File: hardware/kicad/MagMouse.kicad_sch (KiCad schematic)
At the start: 0 parts

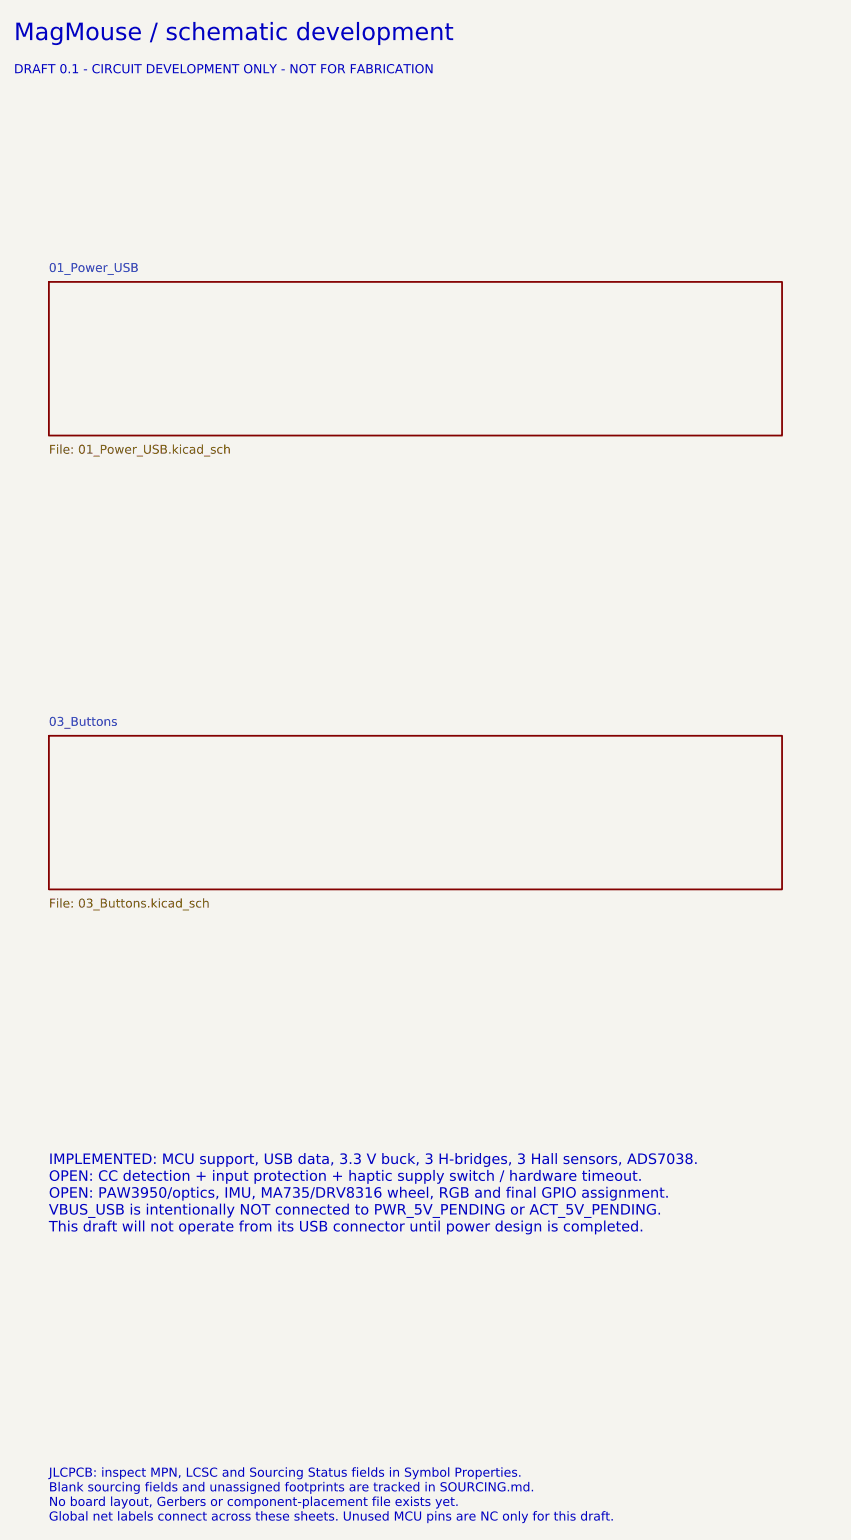
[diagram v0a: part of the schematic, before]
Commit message: Resolve KiCad component sourcing and missing footprints
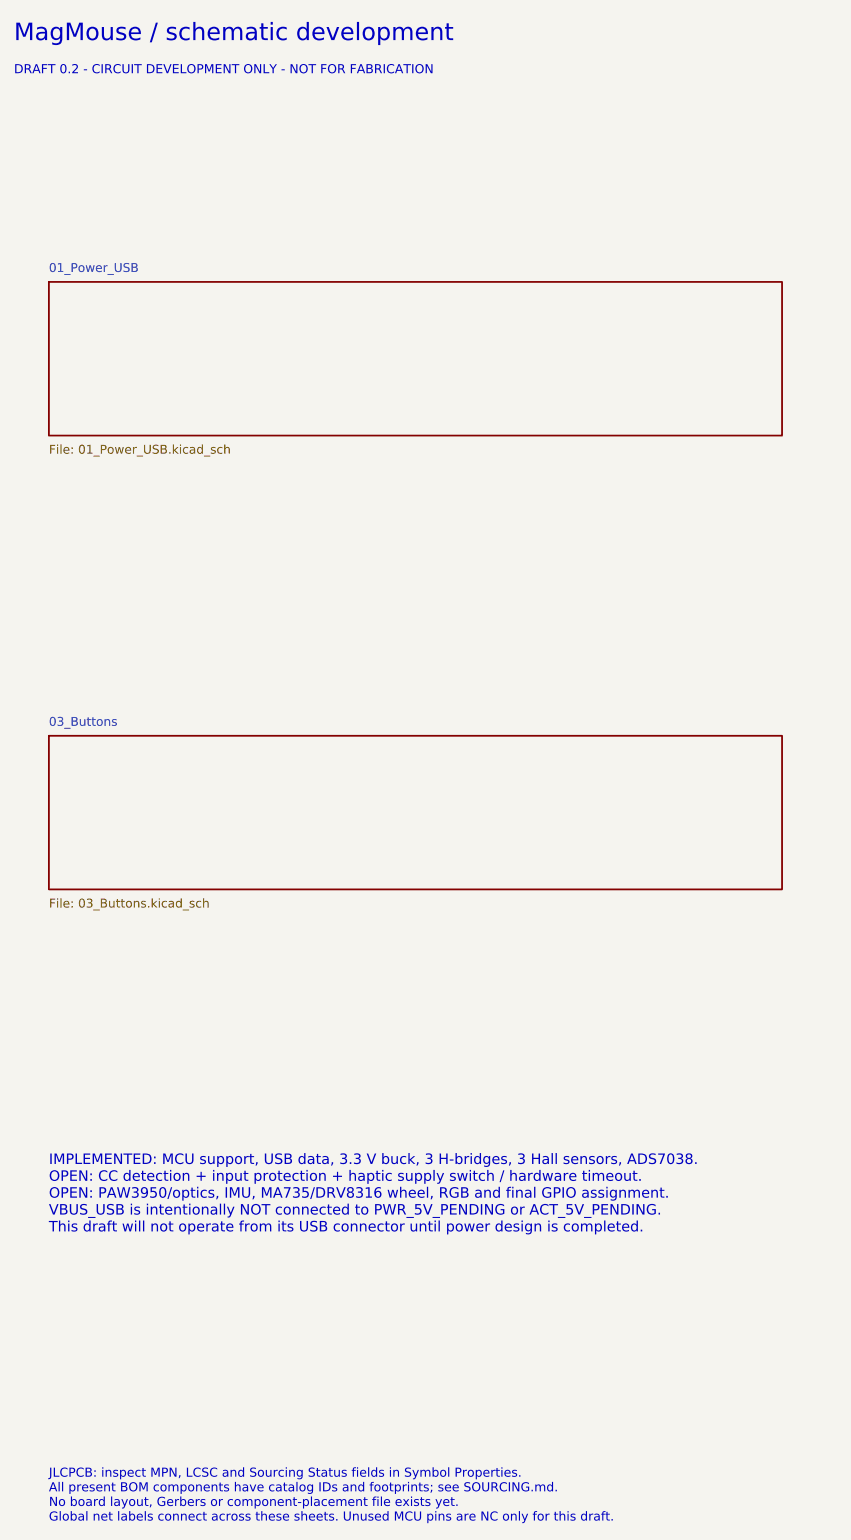
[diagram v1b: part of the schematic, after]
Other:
- note added: "DRAFT 0.2 - CIRCUIT DEVELOPMENT ONLY - NOT FOR FABRICATION"
- note added: "JLCPCB: inspect MPN, LCSC and Sourcing Status fields in Symbol Properties. All present BOM components have catalog IDs and footprints; see SOURCING.md. No board layout, Gerbers or component-placement file exists yet. Global net labels connect across these sheets. Unused MCU pins are NC only for this draft."
- note removed: "DRAFT 0.1 - CIRCUIT DEVELOPMENT ONLY - NOT FOR FABRICATION"
- note removed: "JLCPCB: inspect MPN, LCSC and Sourcing Status fields in Symbol Properties. Blank sourcing fields and unassigned footprints are tracked in SOURCING.md. No board layout, Gerbers or component-placement file exists yet. Global net labels connect across these sheets. Unused MCU pins are NC only for this draft."
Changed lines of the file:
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@@
     (title "MagMouse - MagMouse")
     (date "2026-09-08")
-    (rev "0.1 DRAFT")
+    (rev "0.2 DRAFT")
     (company "MagMouse")
     (comment 1 "NOT FOR FABRICATION - unresolved circuits listed in README.md"))
@@
       (justify left top))
 )
-  (text "DRAFT 0.1 - CIRCUIT DEVELOPMENT ONLY - NOT FOR FABRICATION"
+  (text "DRAFT 0.2 - CIRCUIT DEVELOPMENT ONLY - NOT FOR FABRICATION"
     (at 20 24 0)
     (effects
@@
       (justify left top))
 )
-  (text "JLCPCB: inspect MPN, LCSC and Sourcing Status fields in Symbol Properties.\nBlank sourcing fields and unassigned footprints are tracked in SOURCING.md.\nNo board layout, Gerbers or component-placement file exists yet.\nGlobal net labels connect across these sheets. Unused MCU pins are NC only for this draft."
+  (text "JLCPCB: inspect MPN, LCSC and Sourcing Status fields in Symbol Properties.\nAll present BOM components have catalog IDs and footprints; see SOURCING.md.\nNo board layout, Gerbers or component-placement file exists yet.\nGlobal net labels connect across these sheets. Unused MCU pins are NC only for this draft."
     (at 25 225 0)
     (effects

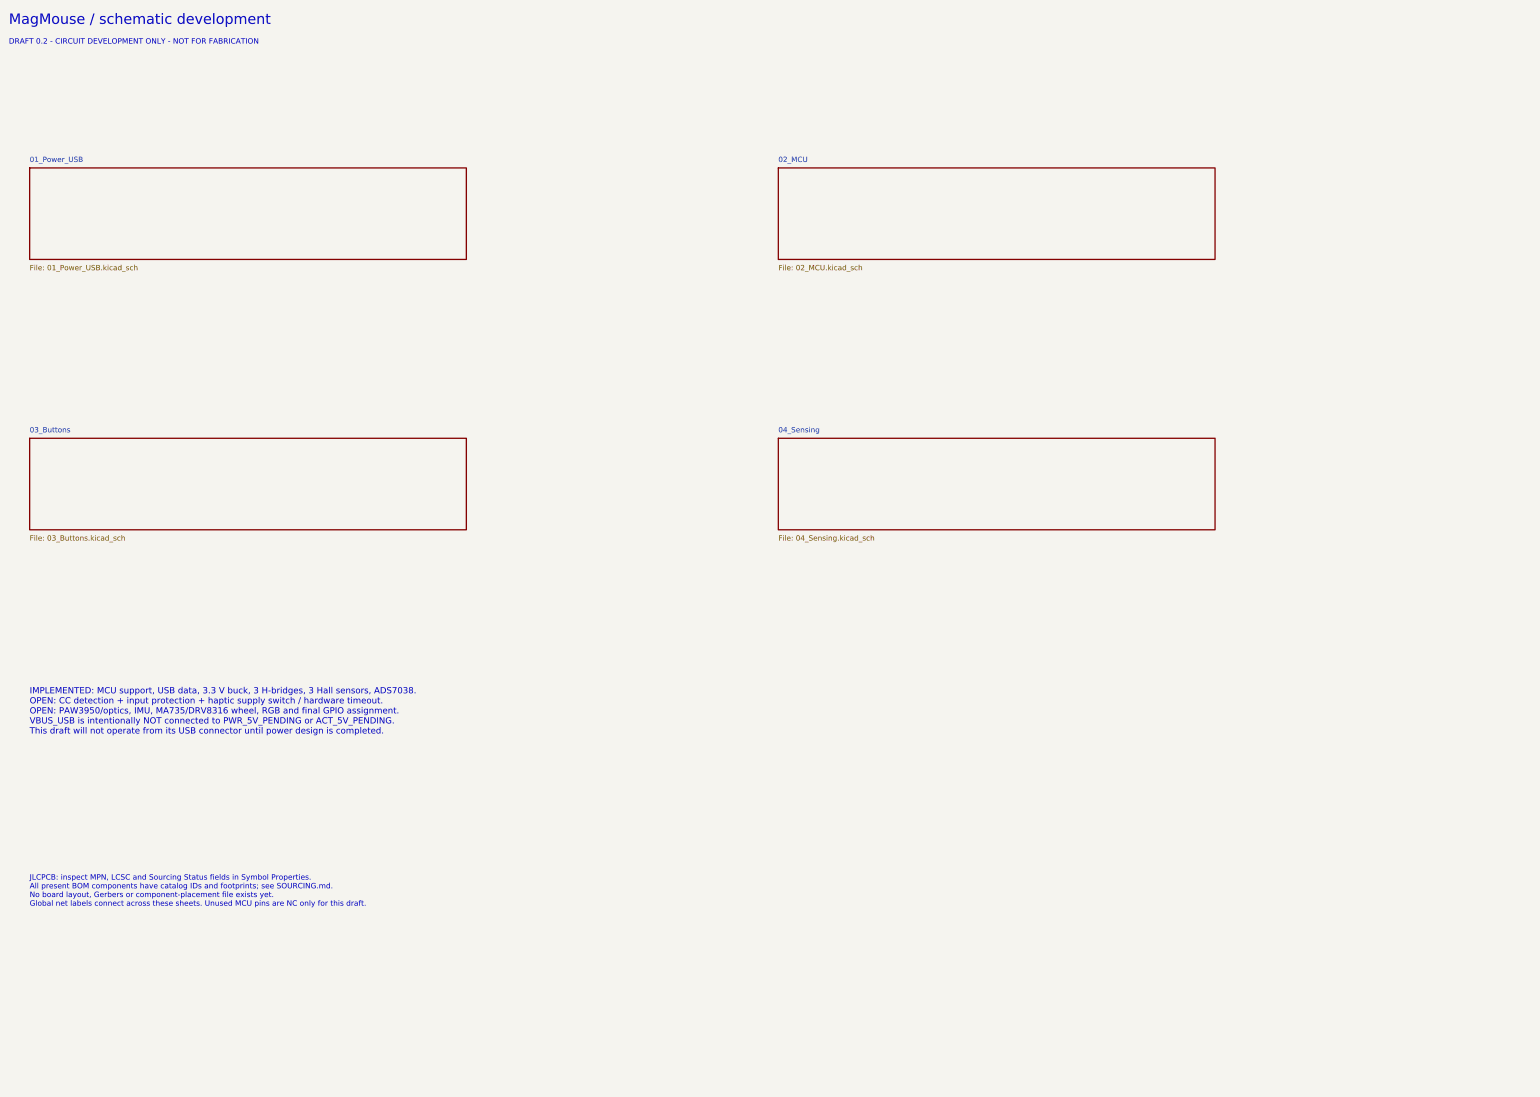
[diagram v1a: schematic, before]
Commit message: Implement USB-C power control schematic and validation
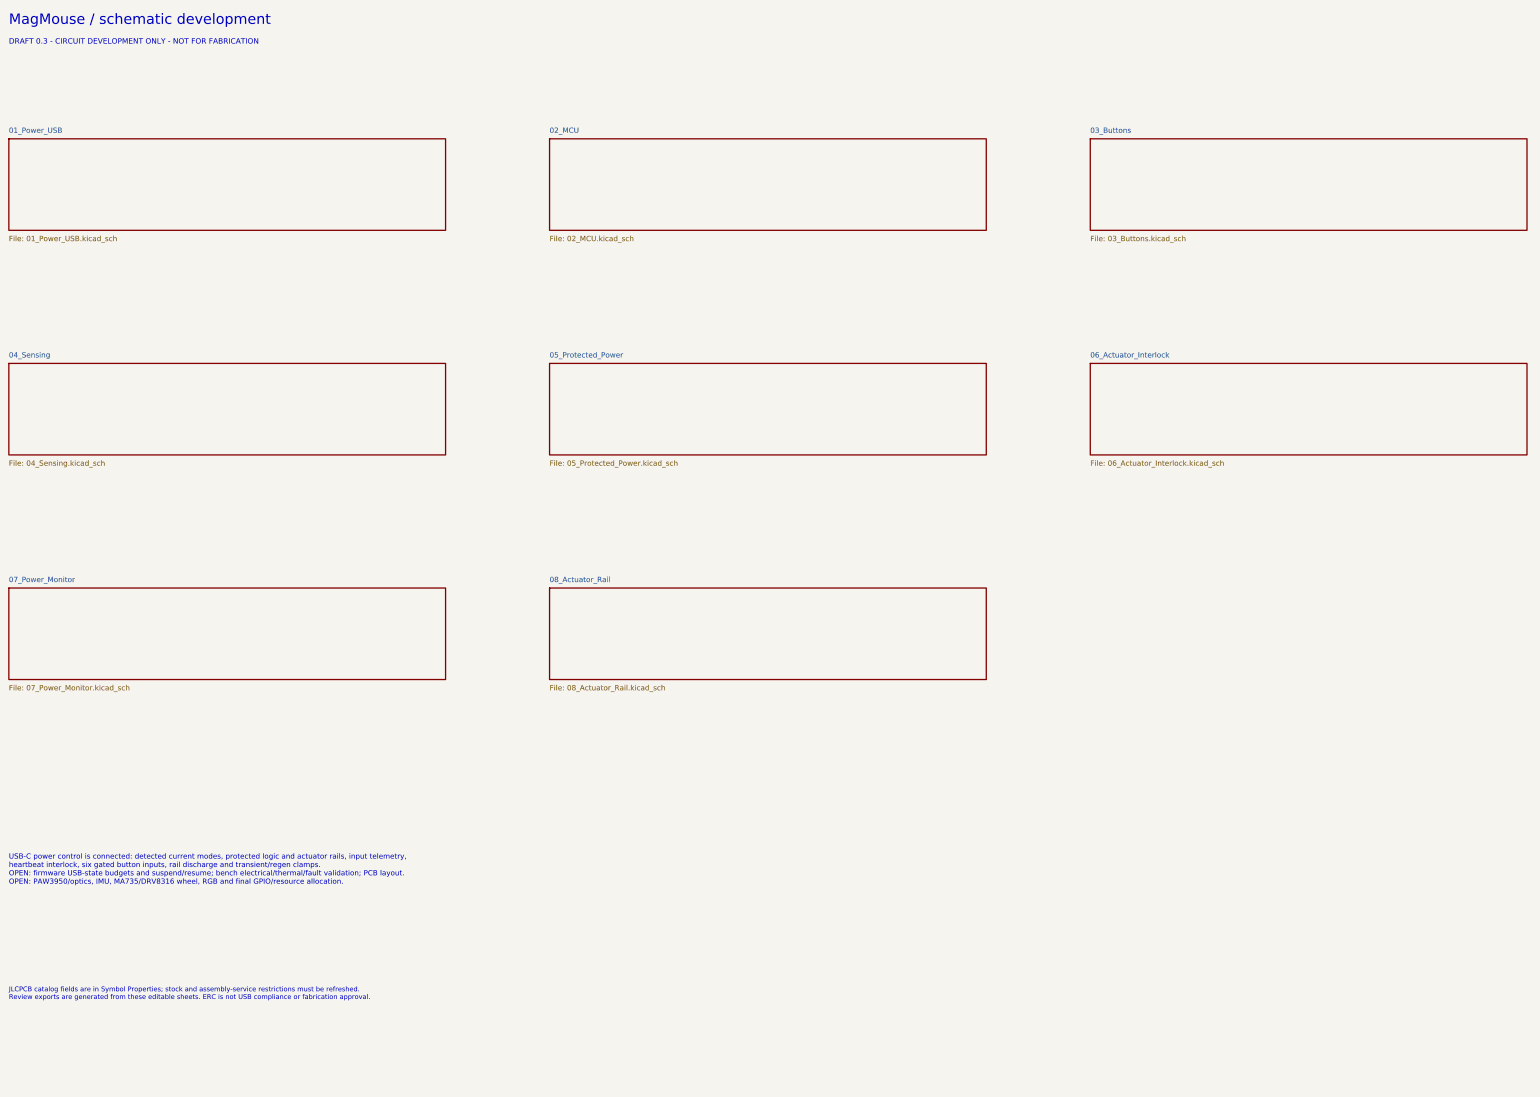
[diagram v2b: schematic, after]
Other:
- added sheet 05_Protected_Power (05_Protected_Power.kicad_sch)
- added sheet 06_Actuator_Interlock (06_Actuator_Interlock.kicad_sch)
- added sheet 07_Power_Monitor (07_Power_Monitor.kicad_sch)
- added sheet 08_Actuator_Rail (08_Actuator_Rail.kicad_sch)
- note added: "DRAFT 0.3 - CIRCUIT DEVELOPMENT ONLY - NOT FOR FABRICATION"
- note added: "JLCPCB catalog fields are in Symbol Properties; stock and assembly-service restrictions must be refreshed. Review exports are generated from these editable sheets. ERC is not USB compliance or fabrication approval."
- note added: "USB-C power control is connected: detected current modes, protected logic and actuator rails, input telemetry, heartbeat interlock, six gated button inputs, rail discharge and transient/regen clamps. OPEN: firmware USB-state budgets and suspend/resume; bench electrical/thermal/fault validation; PCB layout. OPEN: PAW3950/optics, IMU, MA735/DRV8316 wheel, RGB and final GPIO/resource allocation."
- note removed: "DRAFT 0.2 - CIRCUIT DEVELOPMENT ONLY - NOT FOR FABRICATION"
- note removed: "IMPLEMENTED: MCU support, USB data, 3.3 V buck, 3 H-bridges, 3 Hall sensors, ADS7038. OPEN: CC detection + input protection + haptic supply switch / hardware timeout. OPEN: PAW3950/optics, IMU, MA735/DRV8316 wheel, RGB and final GPIO assignment. VBUS_USB is intentionally NOT connected to PWR_5V_PENDING or ACT_5V_PENDING. This draft will not operate from its USB connector until power design is com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"
- note removed: "JLCPCB: inspect MPN, LCSC and Sourcing Status fields in Symbol Properties. All present BOM components have catalog IDs and footprints; see SOURCING.md. No board layout, Gerbers or component-placement file exists yet. Global net labels connect across these sheets. Unused MCU pins are NC only for this draft."
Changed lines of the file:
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@@
     (title "MagMouse - MagMouse")
     (date "2026-09-08")
-    (rev "0.2 DRAFT")
+    (rev "0.3 DRAFT")
     (company "MagMouse")
     (comment 1 "NOT FOR FABRICATION - unresolved circuits listed in README.md"))
@@
       (justify left top))
 )
-  (text "DRAFT 0.2 - CIRCUIT DEVELOPMENT ONLY - NOT FOR FABRICATION"
+  (text "DRAFT 0.3 - CIRCUIT DEVELOPMENT ONLY - NOT FOR FABRICATION"
     (at 20 24 0)
     (effects
@@
 )
   (sheet
-    (at 25 55)
+    (at 20 48)
     (size 105 22)
     (stroke
@@
       (color 0 0 0 0))
     (property "Sheetname" "01_Power_USB"
-      (at 25 53.73 0)
+      (at 20 46.73 0)
       (effects
         (font
@@
         (justify left bottom)))
     (property "Sheetfile" "01_Power_USB.kicad_sch"
-      (at 25 78.27 0)
+      (at 20 71.27 0)
       (effects
         (font
@@
           (page "2")))))
   (sheet
-    (at 205 55)
+    (at 150 48)
     (size 105 22)
     (stroke
@@
       (color 0 0 0 0))
     (property "Sheetname" "02_MCU"
-      (at 205 53.73 0)
+      (at 150 46.73 0)
       (effects
         (font
@@
         (justify left bottom)))
     (property "Sheetfile" "02_MCU.kicad_sch"
-      (at 205 78.27 0)
+      (at 150 71.27 0)
       (effects
         (font
@@
           (page "3")))))
   (sheet
-    (at 25 120)
+    (at 280 48)
     (size 105 22)
     (stroke
@@
       (color 0 0 0 0))
     (property "Sheetname" "03_Buttons"
-      (at 25 118.73 0)
+      (at 280 46.73 0)
       (effects
         (font
@@
         (justify left bottom)))
     (property "Sheetfile" "03_Buttons.kicad_sch"
-      (at 25 143.27 0)
+      (at 280 71.27 0)
       (effects
         (font
@@
           (page "4")))))
   (sheet
-    (at 205 120)
+    (at 20 102)
     (size 105 22)
     (stroke
@@
       (color 0 0 0 0))
     (property "Sheetname" "04_Sensing"
-      (at 205 118.73 0)
+      (at 20 100.73 0)
       (effects
         (font
@@
         (justify left bottom)))
     (property "Sheetfile" "04_Sensing.kicad_sch"
-      (at 205 143.27 0)
+      (at 20 125.27 0)
       (effects
         (font
@@
         (path "/5d73110b-42e6-5c5c-9841-c82d60f67640"
           (page "5")))))
-  (text "IMPLEMENTED: MCU support, USB data, 3.3 V buck, 3 H-bridges, 3 Hall sensors, ADS7038.\nOPEN: CC detection + input protection + haptic supply switch / hardware timeout.\nOPEN: PAW3950/optics, IMU, MA735/DRV8316 wheel, RGB and final GPIO assignment.\nVBUS_USB is intentionally NOT connected to PWR_5V_PENDING or ACT_5V_PENDING.\nThis draft will not operate from its USB connector until power design is completed."
-    (at 25 180 0)
-    (effects
-      (font
-        (size 1.5 1.5))
-      (justify left top))
-)
-  (text "JLCPCB: inspect MPN, LCSC and Sourcing Status fields in Symbol Properties.\nAll present BOM components have catalog IDs and footprints; see SOURCING.md.\nNo board layout, Gerbers or component-placement file exists yet.\nGlobal net labels connect across these sheets. Unused MCU pins are NC only for this draft."
-    (at 25 225 0)
-    (effects
-      (font
-        (size 1.3 1.3))
-      (justify left top))
-)
+  (sheet
+    (at 150 102)
+    (size 105 22)
+    (stroke
+      (width 0.254)
+      (type default))
+    (fill
+      (color 0 0 0 0))
+    (property "Sheetname" "05_Protected_Power"
+      (at 150 100.73 0)
+      (effects
+        (font
+          (size 1.27 1.27))
+        (justify left bottom)))
+    (property "Sheetfile" "05_Protected_Power.kicad_sch"
+      (at 150 125.27 0)
+      (effects
+        (font
+          (size 1.27 1.27))
+        (justify left top)))
+    (instances
+      (project "MagMouse"
+        (path "/5d73110b-42e6-5c5c-9841-c82d60f67640"
+          (page "6")))))
+  (sheet
+    (at 280 102)
+    (size 105 22)
+    (stroke
+      (width 0.254)
+      (type default))
+    (fill
+      (color 0 0 0 0))
+    (property "Sheetname" "06_Actuator_Interlock"
+      (at 280 100.73 0)
+      (effects
+        (font
+          (size 1.27 1.27))
+        (justify left bottom)))
+    (property "Sheetfile" "06_Actuator_Interlock.kicad_sch"
+      (at 280 125.27 0)
+      (effects
+        (font
+          (size 1.27 1.27))
+        (justify left top)))
+    (instances
+      (project "MagMouse"
+        (path "/5d73110b-42e6-5c5c-9841-c82d60f67640"
+          (page "7")))))
+  (sheet
+    (at 20 156)
+    (size 105 22)
+    (stroke
+      (width 0.254)
+      (type default))
+    (fill
+      (color 0 0 0 0))
+    (property "Sheetname" "07_Power_Monitor"
+      (at 20 154.73 0)
+      (effects
+        (font
+          (size 1.27 1.27))
+        (justify left bottom)))
+    (property "Sheetfile" "07_Power_Monitor.kicad_sch"
+      (at 20 179.27 0)
+      (effects
+        (font
+          (size 1.27 1.27))
+        (justify left top)))
+    (instances
+      (project "MagMouse"
+        (path "/5d73110b-42e6-5c5c-9841-c82d60f67640"
+          (page "8")))))
+  (sheet
+    (at 150 156)
+    (size 105 22)
+    (stroke
+      (width 0.254)
+      (type default))
+    (fill
+      (color 0 0 0 0))
+    (property "Sheetname" "08_Actuator_Rail"
+      (at 150 154.73 0)
+      (effects
+        (font
+          (size 1.27 1.27))
+        (justify left bottom)))
+    (property "Sheetfile" "08_Actuator_Rail.kicad_sch"
+      (at 150 179.27 0)
+      (effects
+        (font
+          (size 1.27 1.27))
+        (justify left top)))
+    (instances
+      (project "MagMouse"
+        (path "/5d73110b-42e6-5c5c-9841-c82d60f67640"
+          (page "9")))))
+  (text "USB-C power control is connected: detected current modes, protected logic and actuator rails, input telemetry,\nheartbeat interlock, six gated button inputs, rail discharge and transient/regen clamps.\nOPEN: firmware USB-state budgets and suspend/resume; bench electrical/thermal/fault validation; PCB layout.\nOPEN: PAW3950/optics, IMU, MA735/DRV8316 wheel, RGB and final GPIO/resource allocation."
+    (at 20 220 0)
+    (effects
+      (font
+        (size 1.25 1.25))
+      (justify left top))
+)
+  (text "JLCPCB catalog fields are in Symbol Properties; stock and assembly-service restrictions must be refreshed.\nReview exports are generated from these editable sheets. ERC is not USB compliance or fabrication approval."
+    (at 20 252 0)
+    (effects
+      (font
+        (size 1.15 1.15))
+      (justify left top))
+)
